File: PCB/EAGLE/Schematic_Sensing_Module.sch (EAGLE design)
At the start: 62 parts, among them IC1 MCP3202P, J1 10118192-0001LF, Q1 CSM-7X-DU, SW2 1825910-6, U1 ATMEGA328P-PU, U2_VCC NCP699SN33T1G, U3_VDD NCP699SN33T1G

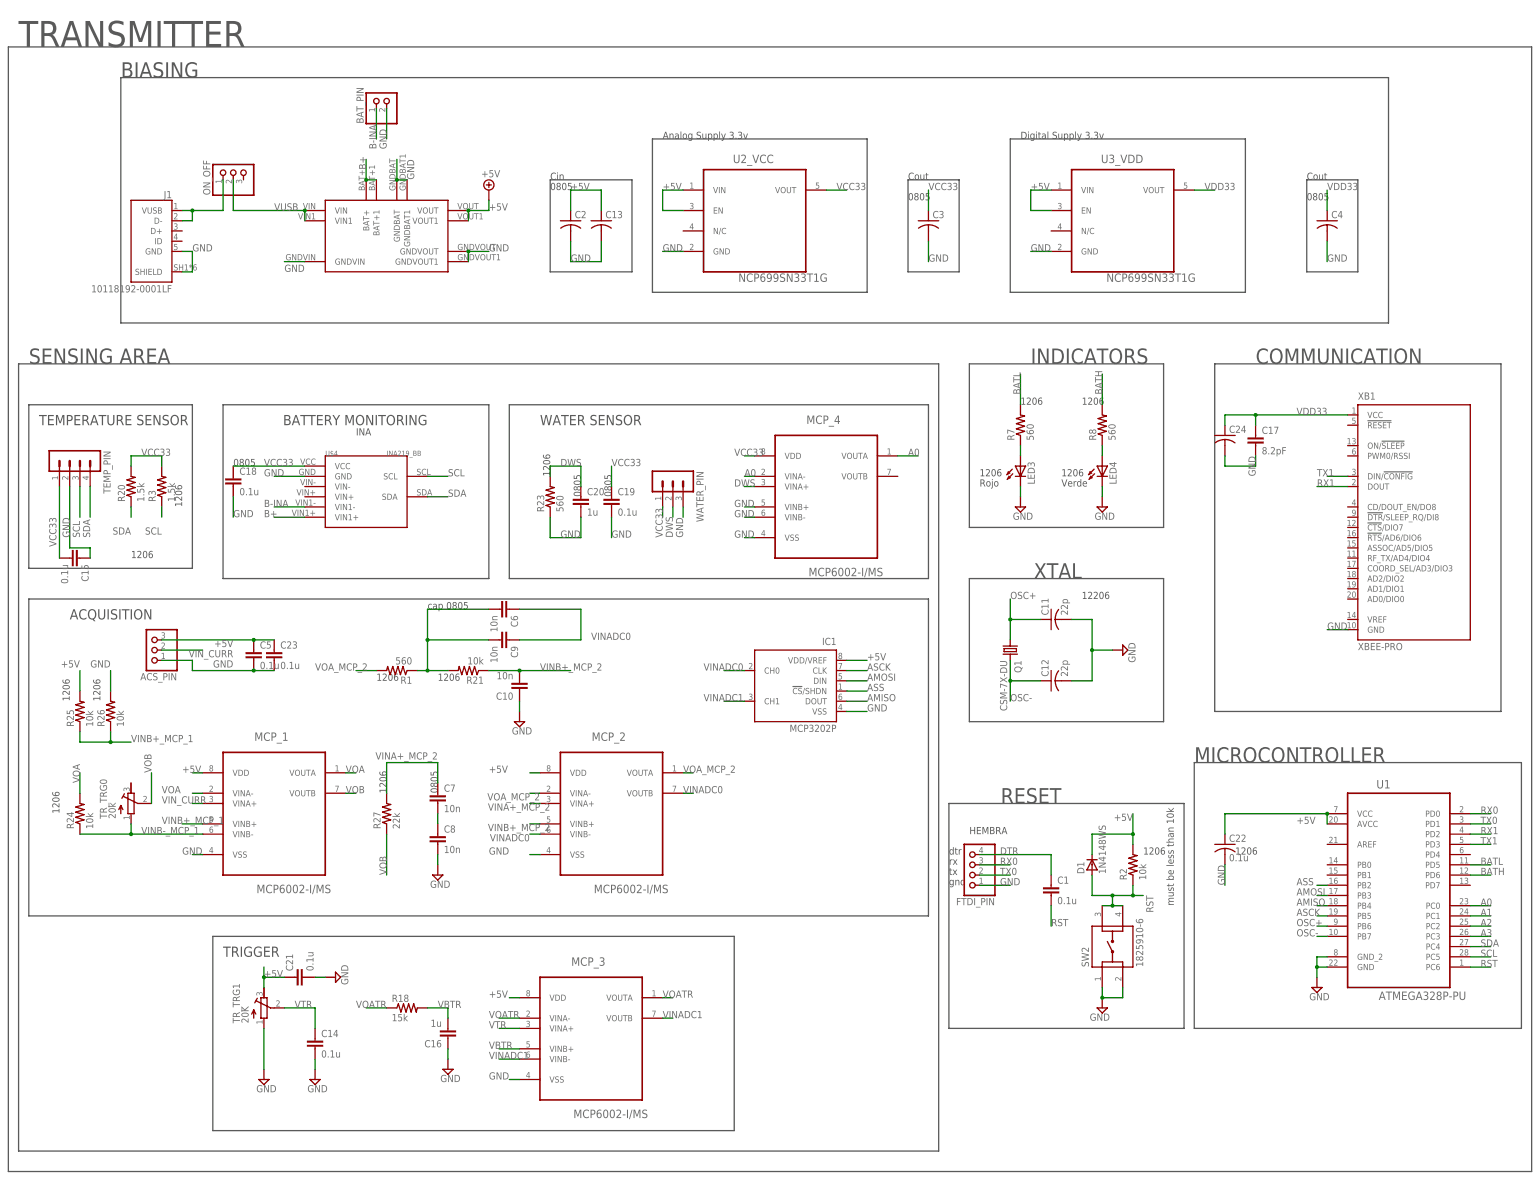
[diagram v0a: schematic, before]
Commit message: adicion de excel de componentes algunas librerias de reguladores en eagle adicion de multiplicador de cap, mod de codigo
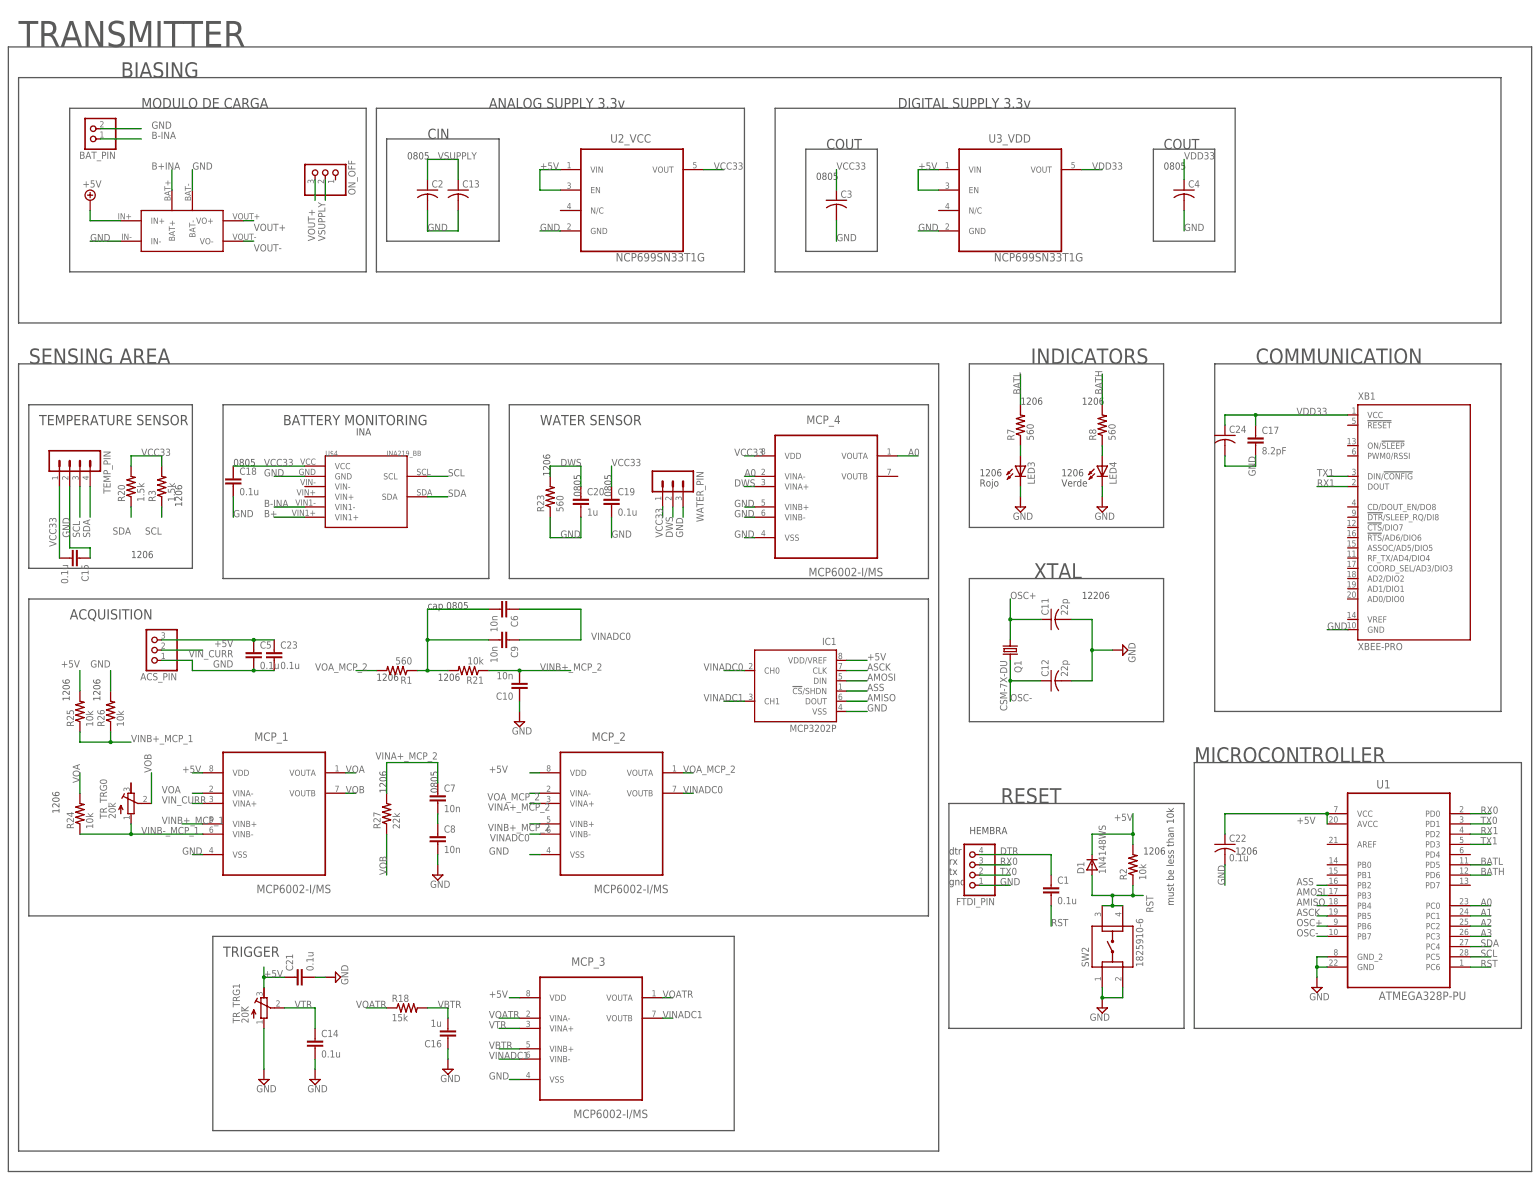
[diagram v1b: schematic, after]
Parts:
- removed J1: 10118192-0001LF, USB-B-2.0:10118192-0001LF
- removed U$2: UPS-LIPO, CHARGER-LIPO-5V:UPS-LIPO
- added U$1: MODULO_CARGA_DEVICE, Modulo_Carga:MODULO_CARGA_DEVICE
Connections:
- removed net N$1: J1.D-, J1.VUSB, ON_OFF.1
- removed net VUSB: ON_OFF.2, U$2.VIN, U$2.VIN1
- new net B+INA: U$1.BAT+
- new net VOUT+: ON_OFF.3, U$1.VO+
- new net VOUT-: U$1.VO-
- new net VSUPPLY: C13.1, C2.1, ON_OFF.2
- net +5V: now also U$1.IN+; no longer C13.1, C2.1, U$2.VOUT, U$2.VOUT1
- net B+: no longer U$2.BAT+, U$2.BAT+1
- net GND: now also U$1.BAT-, U$1.IN-; no longer J1.GND, J1.SHIELD, U$2.GNDBAT, U$2.GNDBAT1, U$2.GNDVIN, U$2.GNDVOUT, U$2.GNDVOUT1
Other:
- note added: "ANALOG SUPPLY 3.3v"
- note added: "CIN"
- note added: "COUT"
- note added: "DIGITAL SUPPLY 3.3v"
- note added: "MODULO DE CARGA"
- note removed: "Analog Supply 3.3v"
- note removed: "Cin"
- note removed: "Cout"
- note removed: "Digital Supply 3.3v"
- moved on the sheet: BAT_PIN, C13, C2, C3, C4, ON_OFF, U2_VCC, U3_VDD
